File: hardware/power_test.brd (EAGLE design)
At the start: 45.2 x 49.3 mm, 53 parts, among them J10 USB-MICROA-AMPHENOL-10118192-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, J3 USB-MICROB-EDAC-690-005-299-0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, U1 DPDT-X2, U2 3.3V, U3 FT232RLSSOP, U4 MCP73831T-2ACI/OT, Y1 P-FET

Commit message: adjust resistor values after some testing.  make GND an High-I net.
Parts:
- R6, R7: value 1K -> 100
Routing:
- net GND: track 91.3 -> 0.00 mm, vias 10 -> 0
- net DTR: track 30.2 -> 0.00 mm
- net FTDI_VCC: track 30.9 -> 7.08 mm, vias 2 -> 0
- net VBUS: track 114.6 -> 91.2 mm, vias 3 -> 0
- net VBAT: track 93.5 -> 70.5 mm, vias 2 -> 0
- net USB_D+: track 21.6 -> 0.00 mm
- net USB_D-: track 20.3 -> 0.00 mm
- net N$14: track 18.5 -> 0.00 mm
- net CTS-1: track 15.6 -> 0.00 mm
- net REG_3V3: track 14.8 -> 0.00 mm
- net 3V3: track 14.2 -> 0.00 mm, vias 2 -> 0
- net FTDI+3V3: track 45.7 -> 31.9 mm, vias 1 -> 0
- net PROG_SEL: track 12.1 -> 0.00 mm
- net RXI-0: track 11.8 -> 0.00 mm
- net RXLED: track 11.5 -> 0.00 mm
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
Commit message: Move pwren pull up to 3.3V rail in accordance with datasheet
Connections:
- net FTDI+3V3: now also R2.1
- net VBUS: no longer R2.1
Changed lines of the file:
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@@
 <wire x1="-40.125" y1="40.5" x2="-40.125" y2="39.125" width="0.127" layer="16"/>
 <wire x1="-61.625" y1="17.625" x2="-61.7" y2="17.6" width="0.127" layer="16"/>
-<wire x1="-37.706" y1="42.325" x2="-30.394" y2="37.125" width="0" layer="19" extent="1-1"/>
-<wire x1="-40.125" y1="40.5" x2="-37.706" y2="42.325" width="0" layer="19" extent="1-16"/>
-<wire x1="-40.8" y1="39.595" x2="-40.125" y2="39.125" width="0" layer="19" extent="1-16"/>
+<contactref element="R2" pad="1"/>
+<wire x1="-40.8" y1="39.595" x2="-60.755" y2="42.9" width="0" layer="19" extent="1-1"/>
+<wire x1="-40.125" y1="39.125" x2="-40.8" y2="39.595" width="0" layer="19" extent="1-16"/>
+<wire x1="-37.706" y1="42.325" x2="-40.125" y2="40.5" width="0" layer="19" extent="1-16"/>
+<wire x1="-30.394" y1="37.125" x2="-37.706" y2="42.325" width="0" layer="19" extent="1-1"/>
 </signal>
 <signal name="N$6">
@@
 <contactref element="5V" pad="1"/>
 <contactref element="D1" pad="A"/>
-<contactref element="R2" pad="1"/>
 <wire x1="-30.25" y1="14.625" x2="-30.25" y2="12.125" width="0.508" layer="16"/>
 <wire x1="-30.25" y1="12.125" x2="-30.2" y2="12.1" width="0.508" layer="16"/>
@@
 <wire x1="-56.85" y1="27.005" x2="-60.1" y2="27.245" width="0" layer="19" extent="1-1"/>
 <wire x1="-62.25" y1="35.75" x2="-64.754" y2="30.95" width="0" layer="19" extent="1-16"/>
-<wire x1="-60.755" y1="42.9" x2="-61.625" y2="42.875" width="0" layer="19" extent="1-16"/>
 <wire x1="-54.4499" y1="35.55" x2="-55.5" y2="35.75" width="0" layer="19" extent="1-16"/>
 <wire x1="-51.75" y1="35.605" x2="-54.4499" y2="35.55" width="0" layer="19" extent="1-1"/>

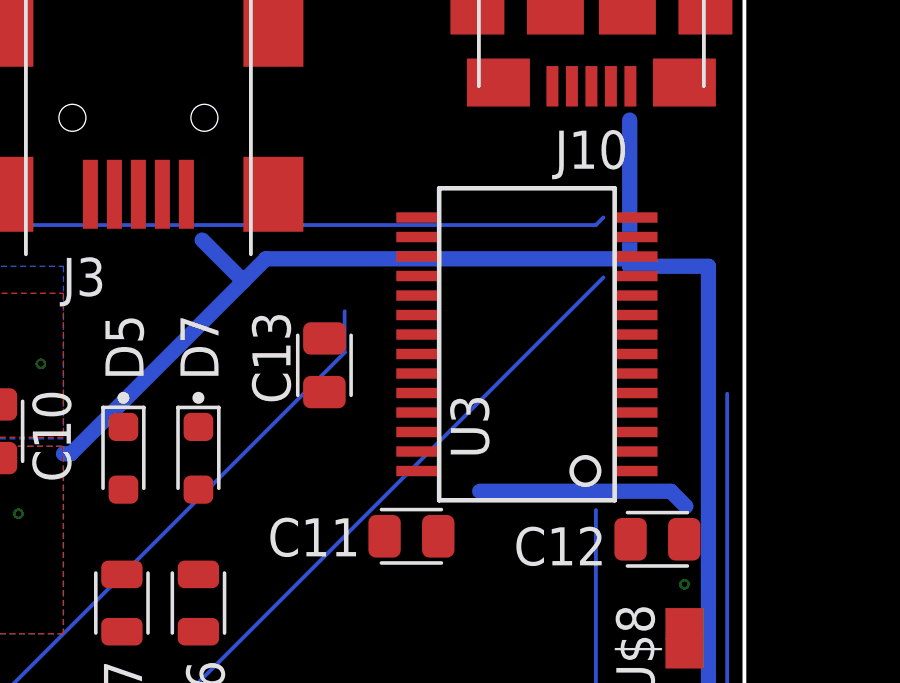
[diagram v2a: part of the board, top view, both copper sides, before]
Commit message: move C13 and FTDI to make it easier to solder on the FTDI.
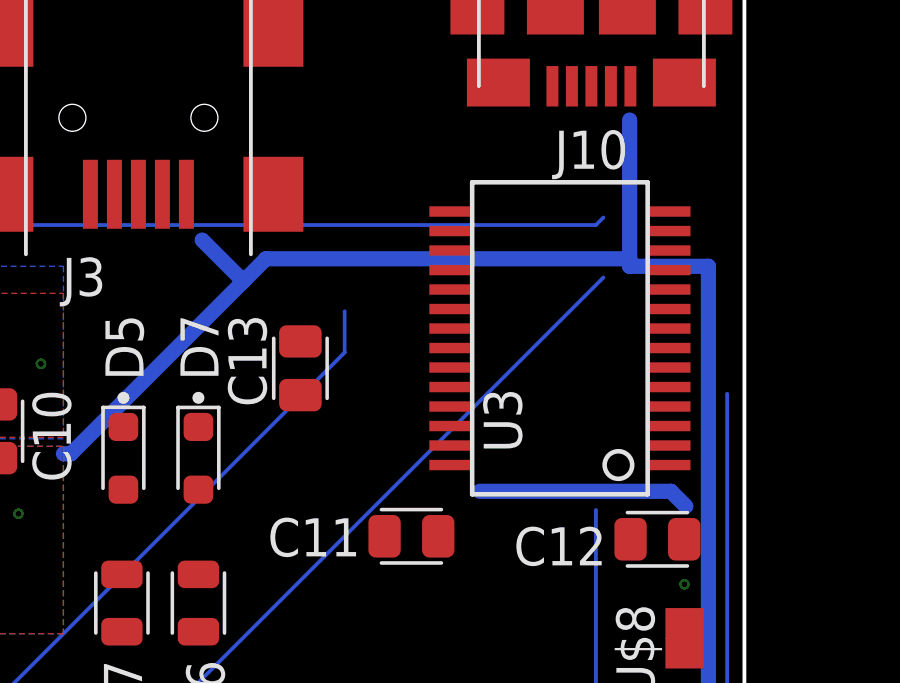
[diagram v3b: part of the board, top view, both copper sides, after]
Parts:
- moved U3 1.12 mm to (-33.0, 39.6)
- moved C13 0.81 mm to (-41.6, 38.6)

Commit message: Preliminary implementation of changes:
Connect VBUS to FTDI directly.
Connect FTDI regulator to 3.3V rail.
Remove mosfet, diode, short across J2.

Still needs clean up to remove uneeded jumpers.
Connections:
- removed net FTDI_VCC: C11.1, C12.1, J5.2, U3.20
- removed net N$4: D1.C, J2.2, S1.B, Y1.D
- net 3V3: now also J1.1
- net BPOS: now also J2.2, S1.B; no longer Y1.S
- net FTDI+3V3: no longer J1.1
- net VBUS: now also C11.1, C12.1, J5.2, U3.20
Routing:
- net FTDI+3V3: track 31.9 -> 0.00 mm
- net 3V3: track 0.00 -> 31.9 mm
- net N$4: track 4.01 -> 0.00 mm
- net BPOS: track 19.4 -> 23.4 mm
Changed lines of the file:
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@@
 <contactref element="3.3V" pad="3"/>
 <contactref element="JP2" pad="3"/>
+<contactref element="J1" pad="1"/>
 <contactref element="J1" pad="2"/>
 <contactref element="R11" pad="2"/>
+<wire x1="-40.125" y1="39.125" x2="-61.625" y2="17.625" width="0.127" layer="16"/>
+<wire x1="-40.125" y1="40.5" x2="-40.125" y2="39.125" width="0.127" layer="16"/>
+<wire x1="-61.625" y1="17.625" x2="-61.7" y2="17.6" width="0.127" layer="16"/>
 <wire x1="-51.9" y1="7.65" x2="-62.63" y2="4.6" width="0" layer="19" extent="1-1"/>
 <wire x1="-45.9283" y1="16.275" x2="-51.9" y2="7.65" width="0" layer="19" extent="1-1"/>
@@
 <wire x1="-33.63" y1="4.65" x2="-34" y2="12.07" width="0" layer="19" extent="1-1"/>
 <wire x1="-59.16" y1="17.6" x2="-51.9" y2="7.65" width="0" layer="19" extent="1-1"/>
-<wire x1="-65.545" y1="25.45" x2="-59.16" y2="17.6" width="0" layer="19" extent="1-1"/>
+<wire x1="-61.625" y1="17.625" x2="-59.16" y2="17.6" width="0" layer="19" extent="16-16"/>
+<wire x1="-65.545" y1="25.45" x2="-61.7" y2="17.6" width="0" layer="19" extent="1-1"/>
 </signal>
 <signal name="VBAT" class="1">
@@
 <contactref element="B1" pad="+"/>
 <contactref element="J2" pad="1"/>
-<contactref element="Y1" pad="S"/>
 <wire x1="-61.75" y1="35" x2="-60.75" y2="34" width="0.508" layer="16"/>
 <wire x1="-63.25" y1="35" x2="-61.75" y2="35" width="0.508" layer="16"/>
@@
 <vertex x="-56" y="29.75"/>
 </polygon>
-<wire x1="-63.25" y1="35" x2="-64.754" y2="32.85" width="0" layer="19" extent="1-16"/>
+<contactref element="S1" pad="B"/>
+<contactref element="J2" pad="2"/>
+<wire x1="-67.25" y1="36.375" x2="-67.25" y2="40.25" width="0.508" layer="16"/>
+<wire x1="-67.25" y1="36.375" x2="-67.14" y2="36.3" width="0.508" layer="16"/>
+<wire x1="-60.75" y1="34" x2="-59" y2="31.75" width="0" layer="19" extent="1-1"/>
 <wire x1="-59.5" y1="35.605" x2="-60.75" y2="34" width="0" layer="19" extent="1-1"/>
 <wire x1="-57.0501" y1="35.55" x2="-59.5" y2="35.605" width="0" layer="19" extent="1-1"/>
-<wire x1="-59" y1="31.75" x2="-60.75" y2="34" width="0" layer="19" extent="1-1"/>
+<wire x1="-67.14" y1="36.3" x2="-64.6" y2="36.3" width="0" layer="19" extent="1-1"/>
+<wire x1="-67.25" y1="41.25" x2="-67.25" y2="40.25" width="0" layer="19" extent="1-16"/>
 </signal>
 <signal name="USB_D-">
@@
 <contactref element="C13" pad="1"/>
 <contactref element="U3" pad="4"/>
-<contactref element="J1" pad="1"/>
-<wire x1="-40.125" y1="39.125" x2="-61.625" y2="17.625" width="0.127" layer="16"/>
-<wire x1="-40.125" y1="40.5" x2="-40.125" y2="39.125" width="0.127" layer="16"/>
-<wire x1="-61.625" y1="17.625" x2="-61.7" y2="17.6" width="0.127" layer="16"/>
 <contactref element="R2" pad="1"/>
 <wire x1="-41.6" y1="39.495" x2="-60.755" y2="42.9" width="0" layer="19" extent="1-1"/>
-<wire x1="-40.125" y1="39.125" x2="-41.6" y2="39.495" width="0" layer="19" extent="1-16"/>
-<wire x1="-36.606" y1="42.525" x2="-40.125" y2="40.5" width="0" layer="19" extent="1-16"/>
+<wire x1="-36.606" y1="42.525" x2="-41.6" y2="39.495" width="0" layer="19" extent="1-1"/>
 <wire x1="-29.294" y1="37.325" x2="-36.606" y2="42.525" width="0" layer="19" extent="1-1"/>
 </signal>
@@
 </signal>
 <signal name="FTDI_VCC" class="1">
-<contactref element="C12" pad="1"/>
-<contactref element="C11" pad="1"/>
-<contactref element="U3" pad="20"/>
-<contactref element="J5" pad="2"/>
 <wire x1="-29.25" y1="34.5" x2="-28.75" y2="34" width="0.508" layer="16"/>
 <wire x1="-35.625" y1="34.5" x2="-29.25" y2="34.5" width="0.508" layer="16"/>
-<wire x1="-37.005" y1="33" x2="-43.8" y2="22.44" width="0" layer="19" extent="1-1"/>
-<wire x1="-35.625" y1="34.5" x2="-37.005" y2="33" width="0" layer="19" extent="1-16"/>
-<wire x1="-28.805" y1="32.9" x2="-28.75" y2="34" width="0" layer="19" extent="1-16"/>
-<wire x1="-36.606" y1="40.575" x2="-35.625" y2="34.5" width="0" layer="19" extent="1-16"/>
 </signal>
 <signal name="VBUS" class="1">
@@
 <wire x1="-30.125" y1="17.375" x2="-30.2" y2="17.18" width="0.508" layer="16"/>
 <wire x1="-30.625" y1="42" x2="-30.625" y2="42.25" width="0.508" layer="16"/>
+<contactref element="C12" pad="1"/>
+<contactref element="C11" pad="1"/>
+<contactref element="U3" pad="20"/>
+<contactref element="J5" pad="2"/>
 <wire x1="-64.754" y1="30.95" x2="-64.335" y2="28.7" width="0" layer="19" extent="1-1"/>
 <wire x1="-60.1" y1="27.245" x2="-64.335" y2="28.7" width="0" layer="19" extent="1-1"/>
@@
 <wire x1="-45.4" y1="44.4" x2="-44.875" y2="42.875" width="0" layer="19" extent="1-16"/>
 <wire x1="-52" y1="31.5" x2="-51" y2="33.75" width="0" layer="19" extent="1-1"/>
+<wire x1="-43.8" y1="22.44" x2="-43.8" y2="19.9" width="0" layer="19" extent="1-1"/>
 <wire x1="-47.55" y1="29.82" x2="-52" y2="31.5" width="0" layer="19" extent="1-1"/>
 <wire x1="-45" y1="29.82" x2="-47.55" y2="29.82" width="0" layer="19" extent="1-1"/>
+<wire x1="-36.606" y1="40.575" x2="-30.625" y2="42" width="0" layer="19" extent="1-16"/>
+<wire x1="-37.005" y1="33" x2="-36.606" y2="40.575" width="0" layer="19" extent="1-1"/>
+<wire x1="-28.805" y1="32.9" x2="-37.005" y2="33" width="0" layer="19" extent="1-1"/>
 </signal>
 <signal name="REG_3V3">
@@
 <wire x1="-29.294" y1="43.825" x2="-31.5" y2="43.625" width="0" layer="19" extent="1-16"/>
 </signal>
-<signal name="N$4" class="1">
-<contactref element="S1" pad="B"/>
-<contactref element="J2" pad="2"/>
-<contactref element="Y1" pad="D"/>
-<contactref element="D1" pad="C"/>
-<wire x1="-67.25" y1="36.375" x2="-67.25" y2="40.25" width="0.508" layer="16"/>
-<wire x1="-67.25" y1="36.375" x2="-67.14" y2="36.3" width="0.508" layer="16"/>
-<wire x1="-67.446" y1="31.9" x2="-67.665" y2="28.7" width="0" layer="19" extent="1-1"/>
-<wire x1="-67.14" y1="36.3" x2="-67.446" y2="31.9" width="0" layer="19" extent="1-1"/>
-<wire x1="-67.25" y1="41.25" x2="-67.25" y2="40.25" width="0" layer="19" extent="1-16"/>
-</signal>
 </signals>

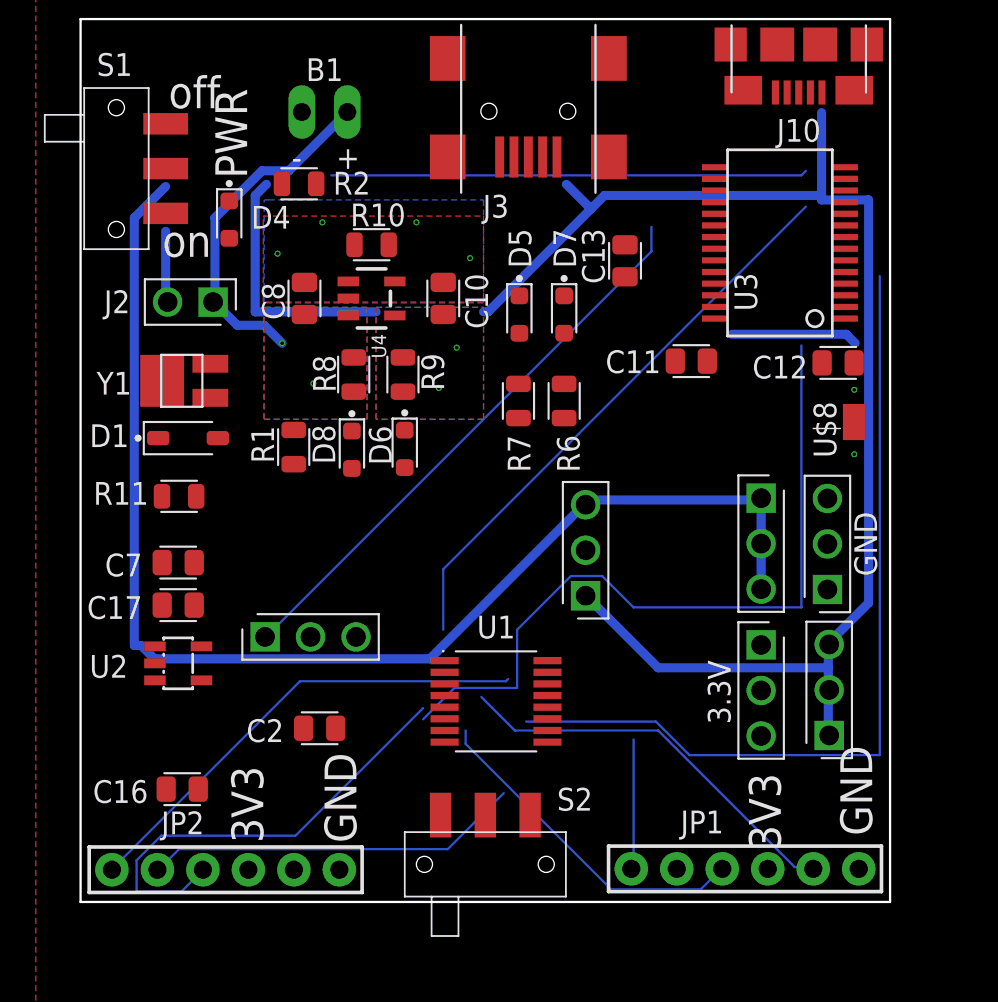
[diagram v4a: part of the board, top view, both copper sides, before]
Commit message: full breakout for battery charger.  remove voltage regulator.  Flip one FTDI port. New source switching scheme.  Remove various jumpers.  Fix Red LEDs
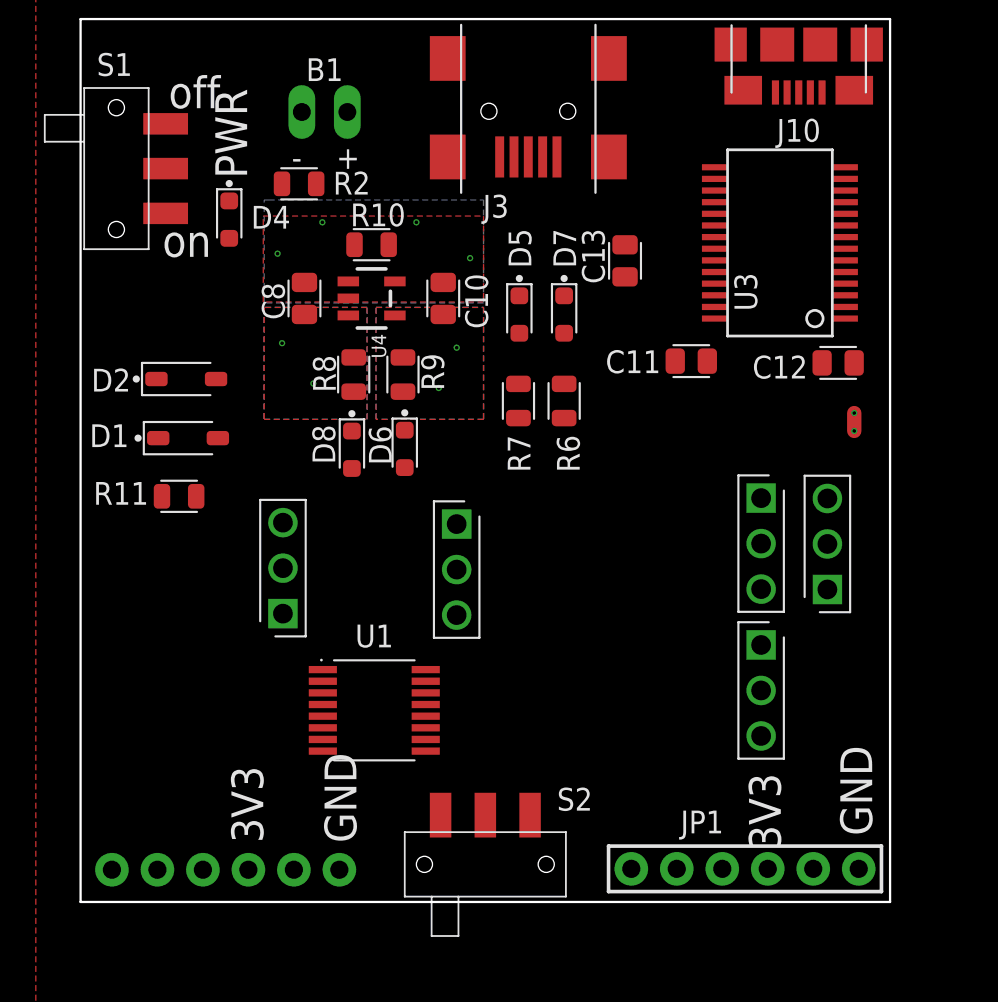
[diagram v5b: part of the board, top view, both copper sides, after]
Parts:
- removed 5V, J1: (no value), Components:HDRV3W63P254_3X1_762X254H838_HS
- removed C16, C17: 1uF, quadparts_prebuilt:CAPC2012X140_HS
- removed C2, C7: 10uF, quadparts_prebuilt:CAPC2012X140_HS
- removed J2: (no value), custom:MALE_HEADER_2X1_0.1IN
- removed R1: 10K, quadparts_prebuilt:RESC2012X60_HS
- removed U2: 3.3V, quadparts_prebuilt:SOT23-DBV
- removed V17, V18: (no value), quadparts_prebuilt:VIA-0.2MM
- removed Y1: P-FET, RemoteParts:FET_SI2302CDS-T1-E3CT-ND
- added D2: 360mV, quadparts_prebuilt:SOD3716X135_HS
- added J4: (no value), Components:HDRV3W63P254_3X1_762X254H838_HS
- R11: value 1K -> 270
- R6, R7: value 100 -> 510
- R8, R9: value 1K -> 510
- moved J5 8.24 mm to (-51.0, 23.9), turned to 270 degrees
- moved U1 6.82 mm to (-55.6, 13.5)
- flipped JP2 to the bottom
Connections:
- removed net FTDI+3V3: C13.1, R2.1, U3.17, U3.4
- removed net REG_3V3: C17.2, C7.1, J1.3, U2.5
- new net N$15: D1.C, S1.B
- net 3V3: now also C13.1, R2.1, U3.17, U3.4; no longer J1.1, J1.2
- net BPOS: now also D1.A, J5.1; no longer J2.1, J2.2, S1.B
- net GND: now also J5.3, U$8.P$1; no longer C16.2, C17.1, C2.2, C7.2, R1.2, U$8.P1, U2.2, V18.P1
- net N$11: now also J4.1
- net N$12: now also J5.2
- net PGND: now also U$8.P$2; no longer U$8.P2, V17.P1
- net VBAT: now also C11.1, C12.1, D2.C, R6.2, R7.2, U3.20; no longer C16.1, C2.1, J5.3, U2.1, U2.3
- net VBUS: now also D2.A, J4.3; no longer 5V.1, 5V.2, 5V.3, C11.1, C12.1, D1.A, J5.1, J5.2, R1.1, R6.2, R7.2, U3.20, Y1.G
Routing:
- net VBUS: track 91.2 -> 0.00 mm
- net VBAT: track 70.5 -> 0.00 mm
- net RXI: track 47.3 -> 0.00 mm
- net TXO: track 41.7 -> 0.00 mm
- net CTS: track 32.0 -> 0.00 mm
- net 3V3: track 31.9 -> 0.00 mm
- net CHR_ENABLE#: track 26.6 -> 0.00 mm
- net DTR-1: track 26.6 -> 0.00 mm
- net TXO-1: track 25.5 -> 0.00 mm
- net BPOS: track 23.4 -> 0.00 mm
- net CTS-0: track 22.5 -> 0.00 mm
- net RXI-1: track 21.1 -> 0.00 mm
- net TXO-0: track 18.9 -> 0.00 mm
- net DTR-0: track 7.35 -> 0.00 mm
- net FTDI_VCC: track 7.08 -> 0.00 mm

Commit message: small changes
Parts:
- added V10, V11, V9: (no value), quadparts_prebuilt:VIA-0.2MM
- moved R11 25.7 mm to (-62.9, 50.9)
- moved R2 25.2 mm to (-36.8, 32.6), turned to 180 degrees
- moved R7 23.3 mm to (-59.2, 50.9), turned to 0 degrees
- moved D2 21.5 mm to (-45.5, 38.3), turned to 90 degrees
- moved VBAT 19.2 mm to (-49.7, 14.3), turned to 0 degrees
- moved D7 17.2 mm to (-38.8, 50.6), turned to 270 degrees
- moved D5 16.3 mm to (-53.0, 50.5), turned to 270 degrees
- moved D8 16.1 mm to (-60.3, 43.3), turned to 270 degrees
- moved R6 15.9 mm to (-39.8, 45.8)
- moved D6 14.9 mm to (-58.8, 41.8)
- moved GND 12.9 mm to (-41.7, 14.3), turned to 0 degrees
- moved D4 10.1 mm to (-66.9, 50.1), turned to 180 degrees
- moved R8 8.91 mm to (-62.2, 39.3), turned to 180 degrees
- moved R9 7.69 mm to (-57.0, 39.3), turned to 0 degrees
- moved C12 5.11 mm to (-28.0, 37.7), turned to 90 degrees
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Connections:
- net 3V3: now also V11.P1
- net VBAT: now also V10.P1
- net VBUS: now also V9.P1
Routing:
- added copper zone on layer 15, net VBAT
- removed copper zone on layer 15, net 3V3
- removed copper zone on layer 1, net PGND
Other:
- board text removed: "PWR"
